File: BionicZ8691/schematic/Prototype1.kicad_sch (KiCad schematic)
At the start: 4 parts, among them J1 BionicConnector, U1 Z86C91, U2 74HCT126

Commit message: Satisfy Electrical Rules Checker
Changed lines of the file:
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@@
   (junction (at 187.96 104.14) (diameter 0) (color 0 0 0 0)
-  )
-  (junction (at 163.83 118.11) (diameter 0) (color 0 0 0 0)
   )
   (junction (at 146.05 118.11) (diameter 0) (color 0 0 0 0)
@@
     (stroke (width 0) (type default) (color 0 0 0 0))
   )
-  (bus_entry (at 143.51 101.6) (size 2.54 2.54)
-    (stroke (width 0) (type default) (color 0 0 0 0))
-  )
   (bus_entry (at 143.51 63.5) (size 2.54 -2.54)
     (stroke (width 0) (type default) (color 0 0 0 0))
@@
     (stroke (width 0) (type default) (color 0 0 0 0))
   )
-  (bus_entry (at 143.51 93.98) (size 2.54 2.54)
-    (stroke (width 0) (type default) (color 0 0 0 0))
-  )
   (bus_entry (at 95.25 86.36) (size -2.54 2.54)
     (stroke (width 0) (type default) (color 0 0 0 0))
@@
     (stroke (width 0) (type default) (color 0 0 0 0))
   )
-  (bus_entry (at 166.37 93.98) (size -2.54 2.54)
-    (stroke (width 0) (type default) (color 0 0 0 0))
-  )
   (bus_entry (at 143.51 53.34) (size 2.54 -2.54)
     (stroke (width 0) (type default) (color 0 0 0 0))
@@
     (stroke (width 0) (type default) (color 0 0 0 0))
   )
-  (bus_entry (at 146.05 132.08) (size -2.54 2.54)
-    (stroke (width 0) (type default) (color 0 0 0 0))
-  )
   (bus_entry (at 143.51 68.58) (size 2.54 -2.54)
     (stroke (width 0) (type default) (color 0 0 0 0))
@@
     (stroke (width 0) (type default) (color 0 0 0 0))
   )
-  (bus_entry (at 196.85 96.52) (size 2.54 2.54)
-    (stroke (width 0) (type default) (color 0 0 0 0))
-  )
   (bus_entry (at 148.59 83.82) (size -2.54 2.54)
     (stroke (width 0) (type default) (color 0 0 0 0))
   )
-  (bus_entry (at 166.37 101.6) (size -2.54 2.54)
-    (stroke (width 0) (type default) (color 0 0 0 0))
-  )
   (bus_entry (at 148.59 78.74) (size -2.54 2.54)
     (stroke (width 0) (type default) (color 0 0 0 0))
@@
     (stroke (width 0) (type default) (color 0 0 0 0))
   )
-  (bus (pts (xy 199.39 91.44) (xy 199.39 99.06))
-    (stroke (width 0) (type default) (color 0 0 0 0))
-  )
   (wire (pts (xy 134.62 60.96) (xy 143.51 60.96))
     (stroke (width 0) (type default) (color 0 0 0 0))
@@
     (stroke (width 0) (type default) (color 0 0 0 0))
   )
-  (bus (pts (xy 163.83 96.52) (xy 163.83 104.14))
-    (stroke (width 0) (type default) (color 0 0 0 0))
-  )
   (bus (pts (xy 199.39 81.28) (xy 199.39 83.82))
     (stroke (width 0) (type default) (color 0 0 0 0))
   )
+  (wire (pts (xy 143.51 106.68) (xy 196.85 106.68))
+    (stroke (width 0) (type default) (color 0 0 0 0))
+  )
   (wire (pts (xy 134.62 142.24) (xy 134.62 144.78))
     (stroke (width 0) (type default) (color 0 0 0 0))
@@
     (stroke (width 0) (type default) (color 0 0 0 0))
   )
+  (wire (pts (xy 196.85 96.52) (xy 187.96 96.52))
+    (stroke (width 0) (type default) (color 0 0 0 0))
+  )
   (bus (pts (xy 163.83 45.72) (xy 163.83 48.26))
     (stroke (width 0) (type default) (color 0 0 0 0))
@@
     (stroke (width 0) (type default) (color 0 0 0 0))
   )
+  (wire (pts (xy 134.62 93.98) (xy 146.05 93.98))
+    (stroke (width 0) (type default) (color 0 0 0 0))
+  )
   (wire (pts (xy 187.96 73.66) (xy 196.85 73.66))
     (stroke (width 0) (type default) (color 0 0 0 0))
@@
     (stroke (width 0) (type default) (color 0 0 0 0))
   )
-  (bus (pts (xy 163.83 118.11) (xy 199.39 118.11))
+  (bus (pts (xy 146.05 118.11) (xy 199.39 118.11))
     (stroke (width 0) (type default) (color 0 0 0 0))
   )
@@
     (stroke (width 0) (type default) (color 0 0 0 0))
   )
-  (bus (pts (xy 146.05 104.14) (xy 146.05 111.76))
-    (stroke (width 0) (type default) (color 0 0 0 0))
-  )
   (wire (pts (xy 134.62 137.16) (xy 134.62 139.7))
     (stroke (width 0) (type default) (color 0 0 0 0))
@@
     (stroke (width 0) (type default) (color 0 0 0 0))
   )
+  (wire (pts (xy 134.62 134.62) (xy 166.37 134.62))
+    (stroke (width 0) (type default) (color 0 0 0 0))
+  )
   (wire (pts (xy 95.25 88.9) (xy 111.76 88.9))
     (stroke (width 0) (type default) (color 0 0 0 0))
@@
     (stroke (width 0) (type default) (color 0 0 0 0))
   )
+  (wire (pts (xy 143.51 101.6) (xy 143.51 106.68))
+    (stroke (width 0) (type default) (color 0 0 0 0))
+  )
   (wire (pts (xy 134.62 129.54) (xy 143.51 129.54))
     (stroke (width 0) (type default) (color 0 0 0 0))
@@
     (stroke (width 0) (type default) (color 0 0 0 0))
   )
+  (wire (pts (xy 196.85 106.68) (xy 196.85 96.52))
+    (stroke (width 0) (type default) (color 0 0 0 0))
+  )
   (wire (pts (xy 119.38 129.54) (xy 101.6 129.54))
     (stroke (width 0) (type default) (color 0 0 0 0))
@@
     (stroke (width 0) (type default) (color 0 0 0 0))
   )
-  (bus (pts (xy 146.05 118.11) (xy 163.83 118.11))
-    (stroke (width 0) (type default) (color 0 0 0 0))
-  )
   (wire (pts (xy 175.26 58.42) (xy 166.37 58.42))
     (stroke (width 0) (type default) (color 0 0 0 0))
@@
     (stroke (width 0) (type default) (color 0 0 0 0))
   )
-  (bus (pts (xy 146.05 96.52) (xy 146.05 99.06))
+  (bus (pts (xy 146.05 93.98) (xy 146.05 99.06))
     (stroke (width 0) (type default) (color 0 0 0 0))
   )
@@
     (stroke (width 0) (type default) (color 0 0 0 0))
   )
-  (bus (pts (xy 146.05 101.6) (xy 146.05 104.14))
+  (bus (pts (xy 146.05 101.6) (xy 146.05 111.76))
     (stroke (width 0) (type default) (color 0 0 0 0))
   )
@@
     (stroke (width 0) (type default) (color 0 0 0 0))
   )
-  (bus (pts (xy 199.39 99.06) (xy 199.39 118.11))
+  (bus (pts (xy 199.39 91.44) (xy 199.39 118.11))
     (stroke (width 0) (type default) (color 0 0 0 0))
   )
@@
     (stroke (width 0) (type default) (color 0 0 0 0))
   )
-  (wire (pts (xy 187.96 96.52) (xy 196.85 96.52))
-    (stroke (width 0) (type default) (color 0 0 0 0))
-  )
   (wire (pts (xy 187.96 50.8) (xy 196.85 50.8))
     (stroke (width 0) (type default) (color 0 0 0 0))
@@
     (stroke (width 0) (type default) (color 0 0 0 0))
   )
-  (bus (pts (xy 146.05 93.98) (xy 146.05 96.52))
-    (stroke (width 0) (type default) (color 0 0 0 0))
-  )
   (wire (pts (xy 175.26 66.04) (xy 166.37 66.04))
     (stroke (width 0) (type default) (color 0 0 0 0))
@@
     (stroke (width 0) (type default) (color 0 0 0 0))
   )
+  (wire (pts (xy 166.37 101.6) (xy 166.37 134.62))
+    (stroke (width 0) (type default) (color 0 0 0 0))
+  )
   (wire (pts (xy 187.96 53.34) (xy 196.85 53.34))
     (stroke (width 0) (type default) (color 0 0 0 0))
@@
     (stroke (width 0) (type default) (color 0 0 0 0))
   )
-  (wire (pts (xy 134.62 134.62) (xy 143.51 134.62))
-    (stroke (width 0) (type default) (color 0 0 0 0))
-  )
   (wire (pts (xy 175.26 45.72) (xy 187.96 45.72))
     (stroke (width 0) (type default) (color 0 0 0 0))
@@
     (stroke (width 0) (type default) (color 0 0 0 0))
   )
-  (bus (pts (xy 146.05 127) (xy 146.05 132.08))
-    (stroke (width 0) (type default) (color 0 0 0 0))
-  )
-  (wire (pts (xy 175.26 93.98) (xy 166.37 93.98))
+  (wire (pts (xy 146.05 93.98) (xy 175.26 93.98))
     (stroke (width 0) (type default) (color 0 0 0 0))
   )
@@
     (stroke (width 0) (type default) (color 0 0 0 0))
   )
-  (bus (pts (xy 163.83 104.14) (xy 163.83 118.11))
-    (stroke (width 0) (type default) (color 0 0 0 0))
-  )
-  (wire (pts (xy 134.62 93.98) (xy 143.51 93.98))
-    (stroke (width 0) (type default) (color 0 0 0 0))
-  )
   (wire (pts (xy 134.62 99.06) (xy 143.51 99.06))
     (stroke (width 0) (type default) (color 0 0 0 0))
@@
     (effects (font (size 1.27 1.27)) (justify left bottom))
   )
+  (label "P1[0..7]" (at 151.13 40.64 0)
+    (effects (font (size 1.27 1.27)) (justify left bottom))
+  )
   (label "P12" (at 137.16 55.88 0)
     (effects (font (size 1.27 1.27)) (justify left bottom))
@@
     (effects (font (size 1.27 1.27)) (justify left bottom))
   )
+  (label "P2[0..7]" (at 151.13 38.1 0)
+    (effects (font (size 1.27 1.27)) (justify left bottom))
+  )
   (label "P53" (at 172.72 101.6 180)
     (effects (font (size 1.27 1.27)) (justify right bottom))
@@
     (effects (font (size 1.27 1.27)) (justify left bottom))
   )
+  (label "P4[0..7]" (at 151.13 118.11 0)
+    (effects (font (size 1.27 1.27)) (justify left bottom))
+  )
   (label "P44" (at 137.16 109.22 0)
     (effects (font (size 1.27 1.27)) (justify left bottom))
@@
   (label "P22" (at 190.5 53.34 0)
     (effects (font (size 1.27 1.27)) (justify left bottom))
-  )
-  (symbol (lib_id "power:VCC") (at -1352.55 -1136.65 0) (unit 1)
-    (in_bom yes) (on_board yes)
-    (property "Reference" "#PWR01" (id 0) (at -1352.55 -1132.84 0)
-      (effects (font (size 1.27 1.27)) hide)
-    )
-    (property "Value" "VCC" (id 1) (at -1352.1182 -1141.0442 0))
-    (property "Footprint" "" (id 2) (at -1352.55 -1136.65 0)
-      (effects (font (size 1.27 1.27)) hide)
-    )
-    (property "Datasheet" "" (id 3) (at -1352.55 -1136.65 0)
-      (effects (font (size 1.27 1.27)) hide)
-    )
-    (pin "1")
   )
   (symbol (lib_id "power:VCC") (at 109.22 102.87 0) (mirror y) (unit 1)
@@
   )
   (symbol_instances
-    (path "/00000000-0000-0000-0000-00005cde46a4"
-      (reference "#PWR01") (unit 1) (value "VCC") (footprint "")
-    )
     (path "/00000000-0000-0000-0000-00006193812c"
       (reference "#PWR02") (unit 1) (value "VCC") (footprint "")

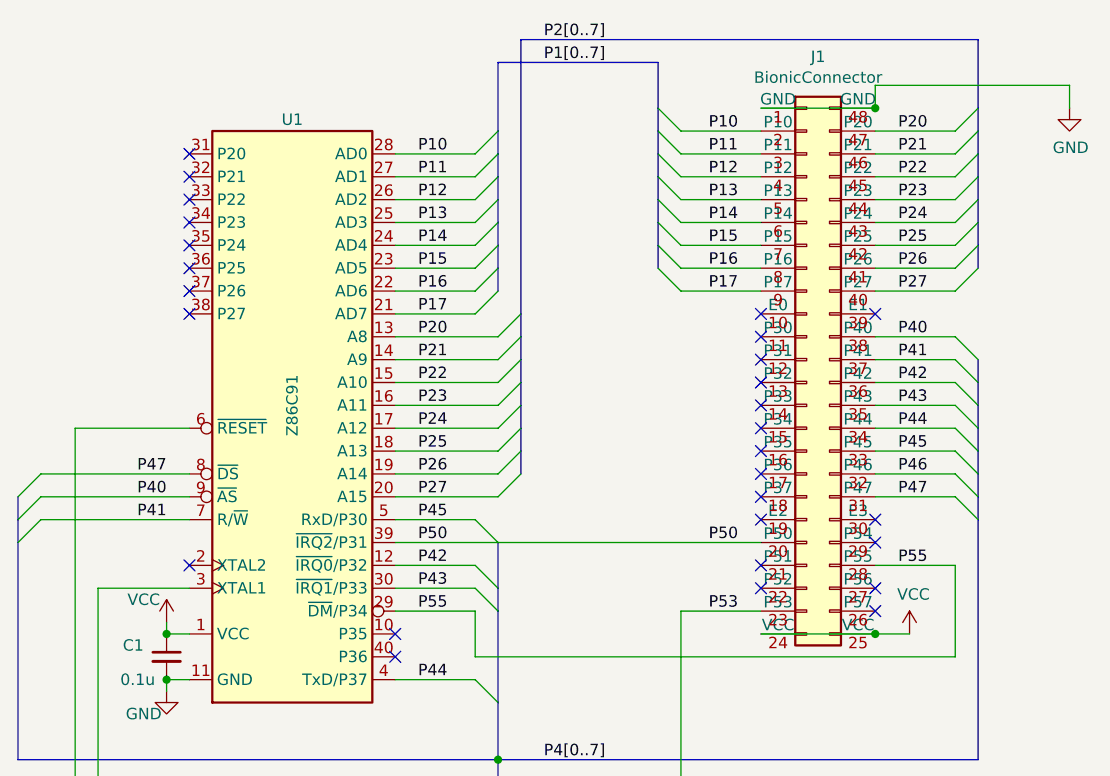
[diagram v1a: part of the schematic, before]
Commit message: [BionicZ8691] Add Port2 connections
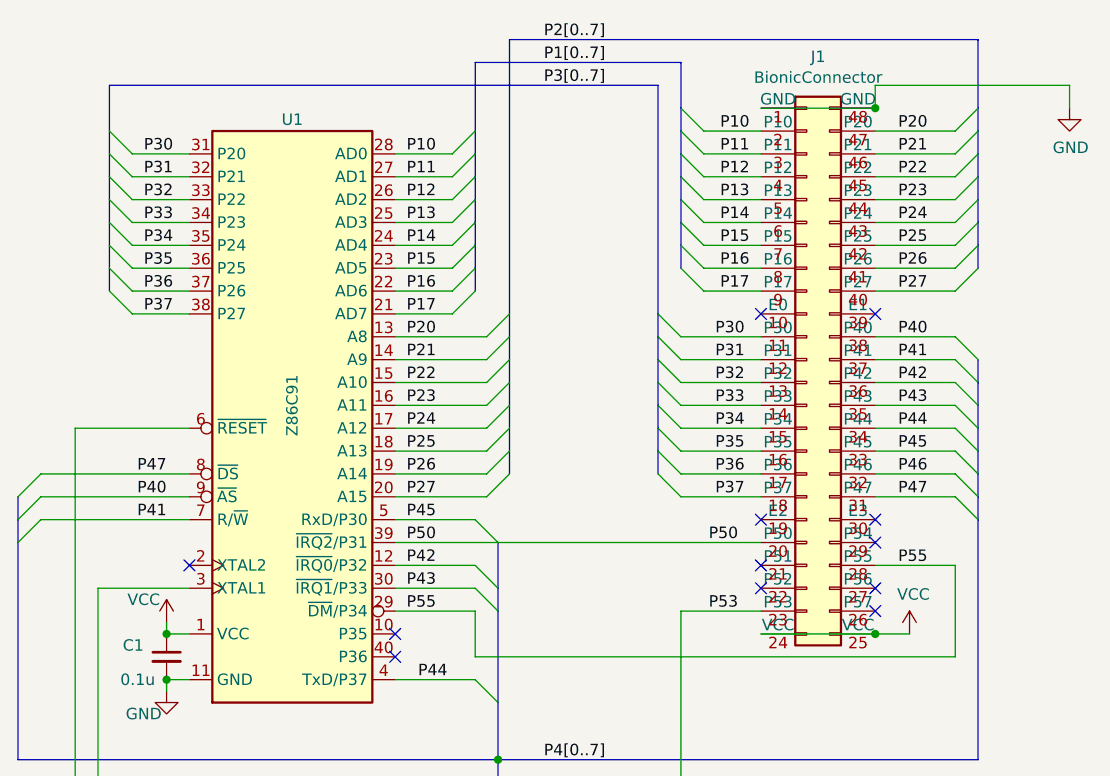
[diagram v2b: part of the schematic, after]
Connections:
- net P30: now reaches U1.31 (P20)
- net P30: now also J1.11 (P30)
- net P31: now reaches U1.32 (P21)
- net P31: now also J1.12 (P31)
- net P32: now reaches U1.33 (P22)
- net P32: now also J1.13 (P32)
- net P33: now reaches U1.34 (P23)
- net P33: now also J1.14 (P33)
- net P34: now reaches U1.35 (P24)
- net P34: now also J1.15 (P34)
- net P35: now reaches U1.36 (P25)
- net P35: now also J1.16 (P35)
- net P36: now reaches U1.37 (P26)
- net P36: now also J1.17 (P36)
- net P37: now reaches U1.38 (P27)
- net P37: now also J1.18 (P37)
- no-connect marks 30 -> 14
